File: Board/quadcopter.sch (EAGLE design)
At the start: 56 parts, among them M1+ TPTP20SQ, M1- TPTP20SQ, M2+ TPTP20SQ, M2- TPTP20SQ, M3+ TPTP20SQ, M3- TPTP20SQ, M4+ TPTP20SQ, M4- TPTP20SQ, U2 LTC1844ES5-3.3TRMPBF, Y1 12MHZ

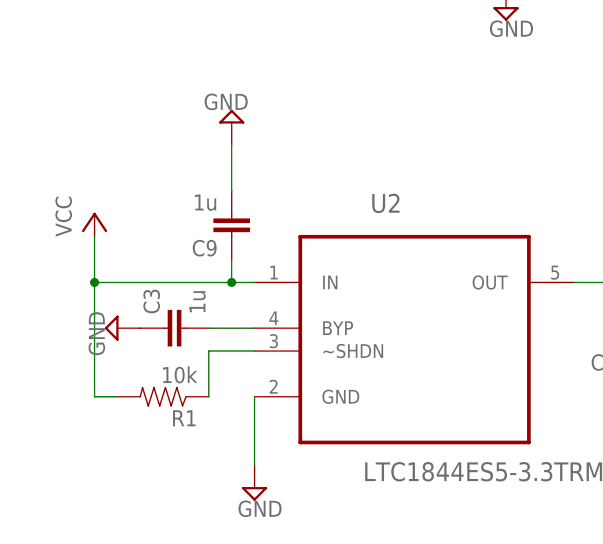
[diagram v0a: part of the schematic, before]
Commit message: Fix in Powersupply
0.1uF instead of 1uF for bypass capacitor
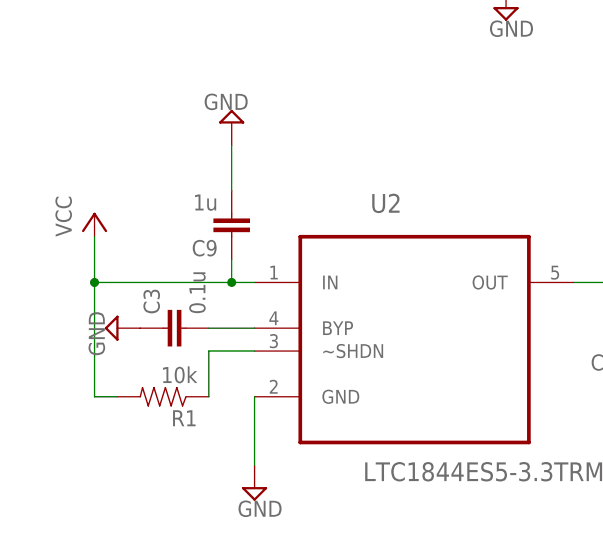
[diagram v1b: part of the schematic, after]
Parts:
- C3: value 1u -> 0.1u
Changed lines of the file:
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@@
 <part name="+3V4" library="supply1" deviceset="+3V3" device=""/>
 <part name="R1" library="SparkFun-Resistors" deviceset="2.0KOHM1/10W5%(0603)" device="" value="10k"/>
-<part name="C3" library="SparkFun-Capacitors" deviceset="10UF-6.3V-20%(0603)" device="" value="1u"/>
+<part name="C3" library="SparkFun-Capacitors" deviceset="10UF-6.3V-20%(0603)" device="" value="0.1u"/>
 <part name="SUPPLY11" library="supply2" deviceset="GND" device=""/>
 <part name="C9" library="SparkFun-Capacitors" deviceset="10UF-6.3V-20%(0603)" device="" value="1u"/>
